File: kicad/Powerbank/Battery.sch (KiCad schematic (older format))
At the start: 4 parts

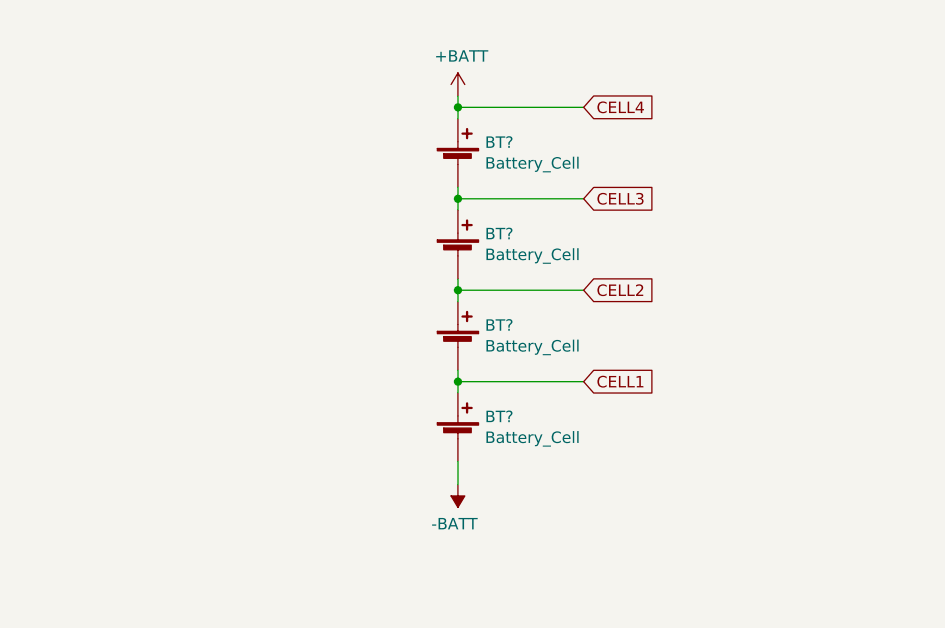
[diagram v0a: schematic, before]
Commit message: Added PD Controller according to reference design
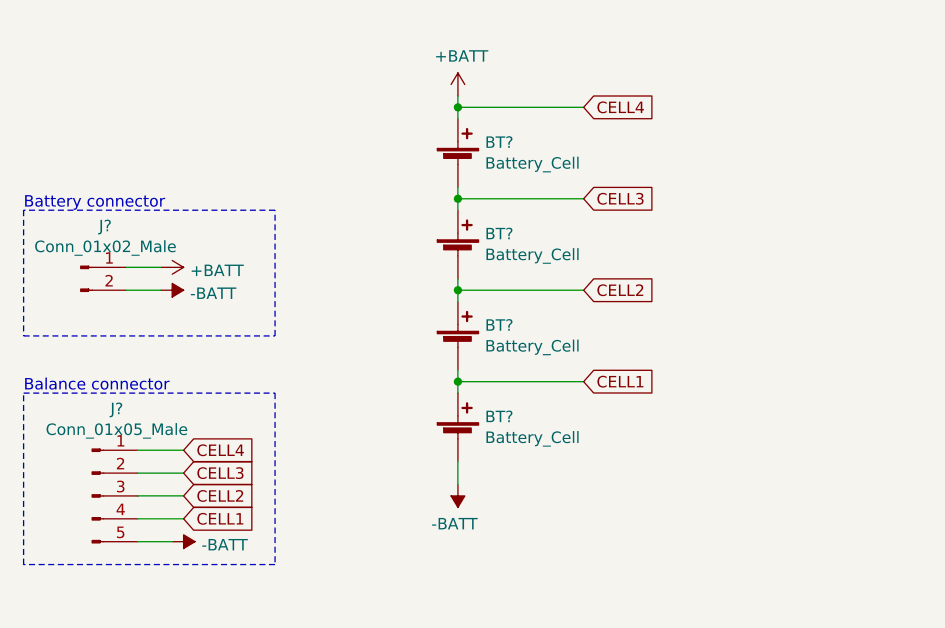
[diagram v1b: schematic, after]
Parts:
- added J?: Conn_01x02_Male, symbol Connector:Conn_01x02_Male
- added J?: Conn_01x05_Male, symbol Connector:Conn_01x05_Male
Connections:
- net +BATT: now also J?.1 (Pin_1), J?.1 (Pin_1)
- net -BATT: now also J?.2 (Pin_2), J?.5 (Pin_5)
- net CELL1: now also J?.4 (Pin_4)
- net CELL2: now also J?.3 (Pin_3)
- net CELL3: now also J?.2 (Pin_2)
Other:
- note added: "Balance connector"
- note added: "Battery connector"
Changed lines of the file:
@@
 $Descr A4 11693 8268
 encoding utf-8
-Sheet 7 7
+Sheet 7 8
 Title ""
 Date ""
@@
 Text GLabel 5500 2800 2    50   Input ~ 0
 CELL4
+$Comp
+L Connector:Conn_01x02_Male J?
+U 1 1 5E810B0B
+P 3300 3500
+F 0 "J?" H 3408 3681 50  0000 C CNN
+F 1 "Conn_01x02_Male" H 3408 3590 50  0000 C CNN
+F 2 "" H 3300 3500 50  0001 C CNN
+F 3 "~" H 3300 3500 50  0001 C CNN
+	1    3300 3500
+	1    0    0    -1
+$EndComp
+$Comp
+L Connector:Conn_01x05_Male J?
+U 1 1 5E81172F
+P 3350 4500
+F 0 "J?" H 3458 4881 50  0000 C CNN
+F 1 "Conn_01x05_Male" H 3458 4790 50  0000 C CNN
+F 2 "" H 3350 4500 50  0001 C CNN
+F 3 "~" H 3350 4500 50  0001 C CNN
+	1    3350 4500
+	1    0    0    -1
+$EndComp
+$Comp
+L power:-BATT #PWR?
+U 1 1 5E812397
+P 3650 3600
+F 0 "#PWR?" H 3650 3450 50  0001 C CNN
+F 1 "-BATT" V 3665 3728 50  0000 L CNN
+F 2 "" H 3650 3600 50  0001 C CNN
+F 3 "" H 3650 3600 50  0001 C CNN
+	1    3650 3600
+	0    1    1    0
+$EndComp
+$Comp
+L power:+BATT #PWR?
+U 1 1 5E812953
+P 3650 3500
+F 0 "#PWR?" H 3650 3350 50  0001 C CNN
+F 1 "+BATT" V 3665 3628 50  0000 L CNN
+F 2 "" H 3650 3500 50  0001 C CNN
+F 3 "" H 3650 3500 50  0001 C CNN
+	1    3650 3500
+	0    1    1    0
+$EndComp
+Wire Wire Line
+	3650 3500 3500 3500
+Wire Wire Line
+	3500 3600 3650 3600
+$Comp
+L power:-BATT #PWR?
+U 1 1 5E813978
+P 3700 4700
+F 0 "#PWR?" H 3700 4550 50  0001 C CNN
+F 1 "-BATT" V 3715 4828 50  0000 L CNN
+F 2 "" H 3700 4700 50  0001 C CNN
+F 3 "" H 3700 4700 50  0001 C CNN
+	1    3700 4700
+	0    1    1    0
+$EndComp
+Wire Wire Line
+	3700 4700 3550 4700
+Text GLabel 3750 4600 2    50   Input ~ 0
+CELL1
+Text GLabel 3750 4500 2    50   Input ~ 0
+CELL2
+Text GLabel 3750 4400 2    50   Input ~ 0
+CELL3
+Wire Wire Line
+	3550 4400 3750 4400
+Wire Wire Line
+	3550 4500 3750 4500
+Wire Wire Line
+	3750 4600 3550 4600
+Text GLabel 3750 4300 2    50   Input ~ 0
+CELL4
+Wire Wire Line
+	3550 4300 3750 4300
+Text Notes 3050 4050 0    50   ~ 0
+Balance connector
+Wire Notes Line
+	3050 4050 4150 4050
+Wire Notes Line
+	4150 4050 4150 4800
+Wire Notes Line
+	4150 4800 3050 4800
+Wire Notes Line
+	3050 4800 3050 4050
+Text Notes 3050 3250 0    50   ~ 0
+Battery connector
+Wire Notes Line
+	3050 3250 3050 3800
+Wire Notes Line
+	3050 3800 4150 3800
+Wire Notes Line
+	4150 3800 4150 3250
+Wire Notes Line
+	4150 3250 3050 3250
 $EndSCHEMATC

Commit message: Updated for PCB
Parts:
- J4: renamed from J?; footprint (none) -> Connector_JST:JST_ZE_BM05B-ZESS-TBT_1x05-1MP_P1.50mm_Vertical
- gave numbers to parts that had none: 5
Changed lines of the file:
@@
 EESchema Schematic File Version 4
+LIBS:Powerbank-cache
 EELAYER 30 0
 EELAYER END
 $Descr A4 11693 8268
 encoding utf-8
-Sheet 7 7
+Sheet 6 7
 Title ""
 Date ""
@@
 $EndDescr
 $Comp
-L Device:Battery_Cell BT?
+L Device:Battery_Cell BT4
 U 1 1 5E0D2631
 P 4950 4250
-F 0 "BT?" H 5068 4346 50  0000 L CNN
+F 0 "BT4" H 5068 4346 50  0000 L CNN
 F 1 "Battery_Cell" H 5068 4255 50  0000 L CNN
 F 2 "" V 4950 4310 50  0001 C CNN
@@
 $EndComp
 $Comp
-L Device:Battery_Cell BT?
+L Device:Battery_Cell BT3
 U 1 1 5E0D2E8A
 P 4950 3850
-F 0 "BT?" H 5068 3946 50  0000 L CNN
+F 0 "BT3" H 5068 3946 50  0000 L CNN
 F 1 "Battery_Cell" H 5068 3855 50  0000 L CNN
 F 2 "" V 4950 3910 50  0001 C CNN
@@
 $EndComp
 $Comp
-L Device:Battery_Cell BT?
+L Device:Battery_Cell BT2
 U 1 1 5E0D30C8
 P 4950 3450
-F 0 "BT?" H 5068 3546 50  0000 L CNN
+F 0 "BT2" H 5068 3546 50  0000 L CNN
 F 1 "Battery_Cell" H 5068 3455 50  0000 L CNN
 F 2 "" V 4950 3510 50  0001 C CNN
@@
 $EndComp
 $Comp
-L Device:Battery_Cell BT?
+L Device:Battery_Cell BT1
 U 1 1 5E0D32C3
 P 4950 3050
-F 0 "BT?" H 5068 3146 50  0000 L CNN
+F 0 "BT1" H 5068 3146 50  0000 L CNN
 F 1 "Battery_Cell" H 5068 3055 50  0000 L CNN
 F 2 "" V 4950 3110 50  0001 C CNN
@@
 CELL4
 $Comp
-L Connector:Conn_01x02_Male J?
+L Connector:Conn_01x02_Male J3
 U 1 1 5E810B0B
 P 3300 3500
-F 0 "J?" H 3408 3681 50  0000 C CNN
+F 0 "J3" H 3408 3681 50  0000 C CNN
 F 1 "Conn_01x02_Male" H 3408 3590 50  0000 C CNN
 F 2 "" H 3300 3500 50  0001 C CNN
@@
 $EndComp
 $Comp
-L Connector:Conn_01x05_Male J?
+L Connector:Conn_01x05_Male J4
 U 1 1 5E81172F
 P 3350 4500
-F 0 "J?" H 3458 4881 50  0000 C CNN
+F 0 "J4" H 3458 4881 50  0000 C CNN
 F 1 "Conn_01x05_Male" H 3458 4790 50  0000 C CNN
-F 2 "" H 3350 4500 50  0001 C CNN
+F 2 "Connector_JST:JST_ZE_BM05B-ZESS-TBT_1x05-1MP_P1.50mm_Vertical" H 3350 4500 50  0001 C CNN
 F 3 "~" H 3350 4500 50  0001 C CNN
 	1    3350 4500

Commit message: Added footprint for all, moved to a first attempt for routing
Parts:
- J3: footprint (none) -> Powerbank:XT30PW-M
- J4: footprint Connector_JST:JST_ZE_BM05B-ZESS-TBT_1x05-1MP_P1.50mm_Vertical -> Connector_JST:JST_ZE_S05B-ZESK-2D_1x05_P1.50mm_Horizontal
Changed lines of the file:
@@
 F 0 "J3" H 3408 3681 50  0000 C CNN
 F 1 "Conn_01x02_Male" H 3408 3590 50  0000 C CNN
-F 2 "" H 3300 3500 50  0001 C CNN
+F 2 "Powerbank:XT30PW-M" H 3300 3500 50  0001 C CNN
 F 3 "~" H 3300 3500 50  0001 C CNN
 	1    3300 3500
@@
 F 0 "J4" H 3458 4881 50  0000 C CNN
 F 1 "Conn_01x05_Male" H 3458 4790 50  0000 C CNN
-F 2 "Connector_JST:JST_ZE_BM05B-ZESS-TBT_1x05-1MP_P1.50mm_Vertical" H 3350 4500 50  0001 C CNN
+F 2 "Connector_JST:JST_ZE_S05B-ZESK-2D_1x05_P1.50mm_Horizontal" H 3350 4500 50  0001 C CNN
 F 3 "~" H 3350 4500 50  0001 C CNN
 	1    3350 4500

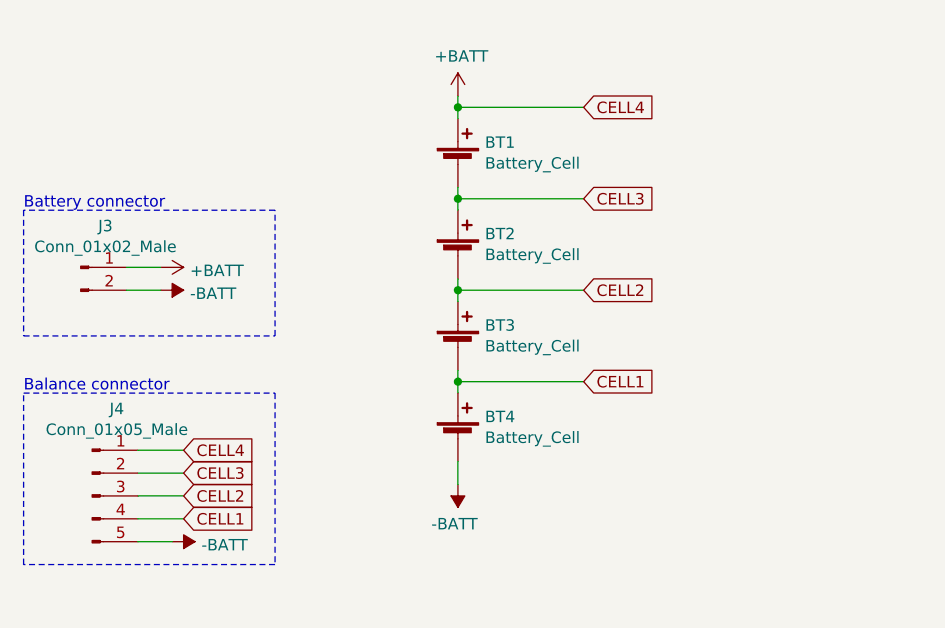
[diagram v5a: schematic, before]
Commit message: Updated layout in schematic for nicer look
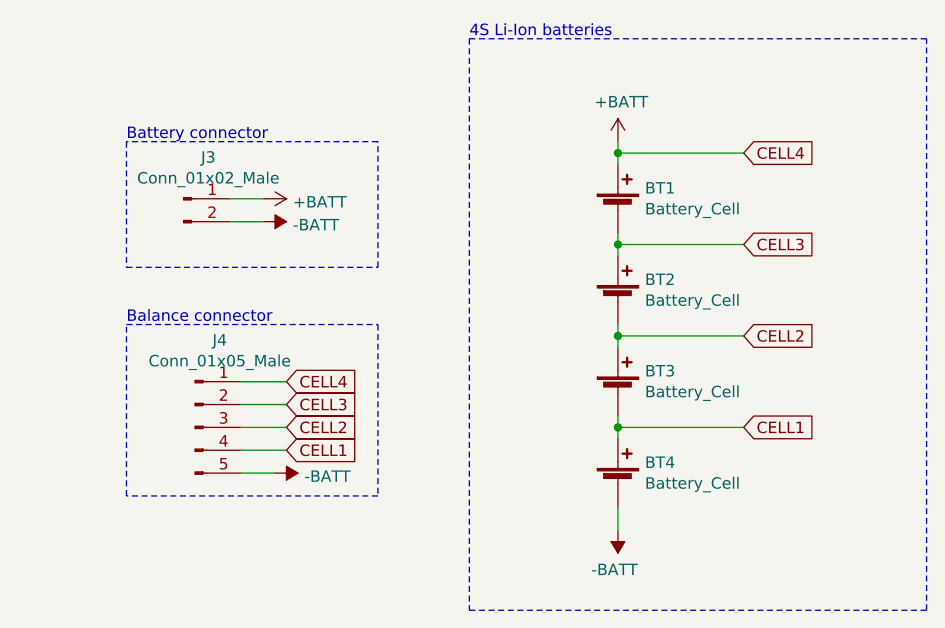
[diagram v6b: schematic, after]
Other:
- note added: "4S Li-Ion batteries"
- moved on the sheet: BT1, BT2, BT3, BT4, J3, J4
